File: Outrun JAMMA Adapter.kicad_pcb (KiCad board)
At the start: 2 copper layers, 111 x 86.6 mm, 31 parts, among them U1 LM386, U2 MCP4902, U3 ATMEGA328

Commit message: tooling holes
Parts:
- added REF**: ToolingHole_1.152mm, MountingHole:ToolingHole_1.152mm, F.Cu at (198.2, 79.4)
- added REF**: ToolingHole_1.152mm, MountingHole:ToolingHole_1.152mm, F.Cu at (99.8, 138.2)
- added REF**: ToolingHole_1.152mm, MountingHole:ToolingHole_1.152mm, F.Cu at (198.2, 138.2)

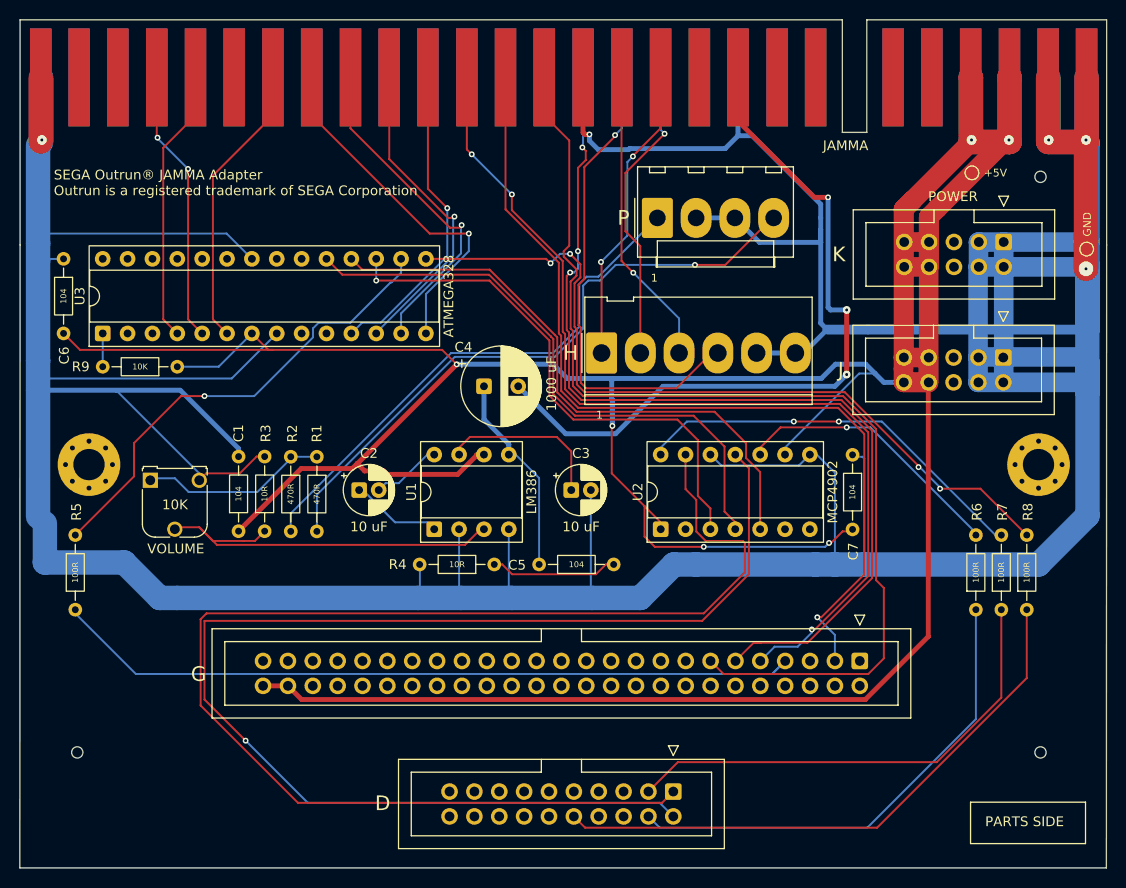
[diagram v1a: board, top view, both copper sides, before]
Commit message: remove tooling holes (0.2 precision), add space
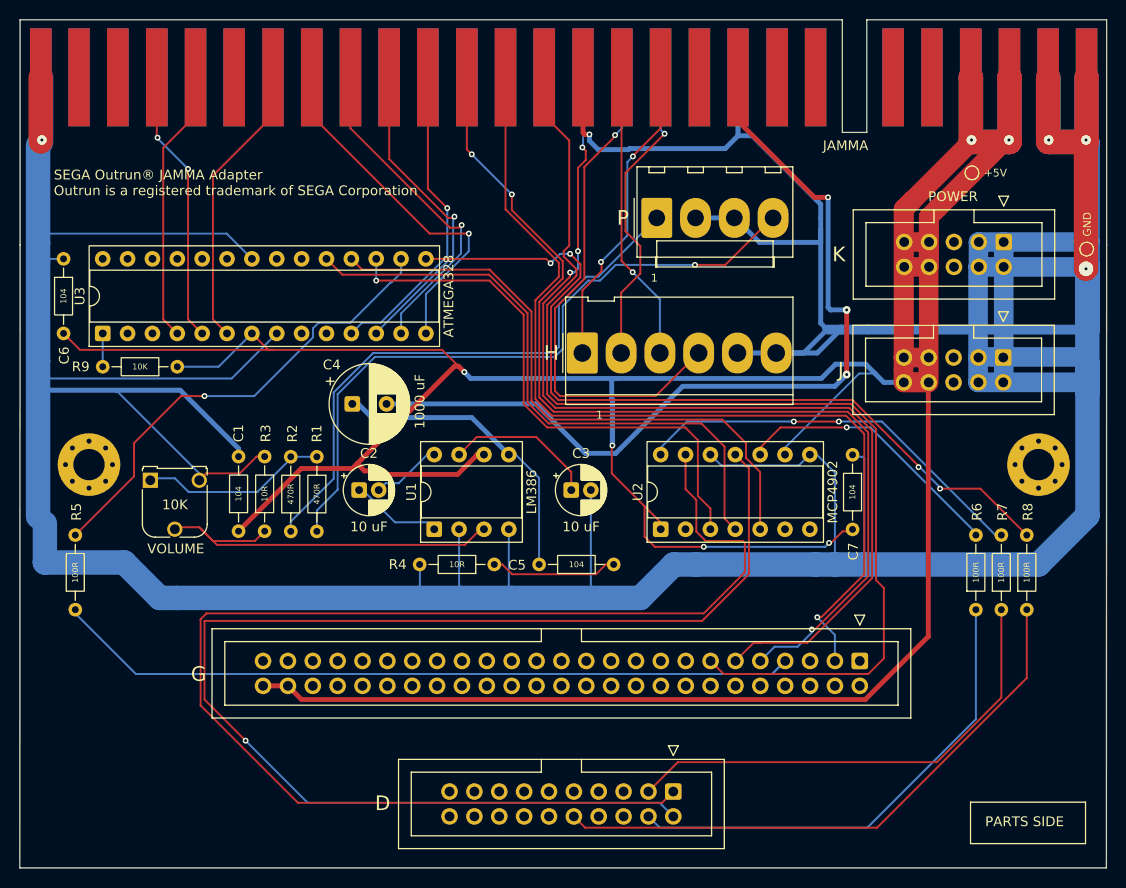
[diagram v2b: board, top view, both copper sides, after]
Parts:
- removed the REF** at (198.2, 79.4)
- removed the REF** at (99.8, 138.2)
- removed the REF** at (198.2, 138.2)
- moved C4 13.6 mm to (127.9, 102.6)
- moved H 1.96 mm to (151.4, 97.4)
- moved P 0.06 mm to (159.0, 83.6)
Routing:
- net SPKR+: track 74.8 -> 89.2 mm
- net PREAMP_OUT: track 20.9 -> 31.0 mm
- net GND: track 603.3 -> 612.9 mm
- net AUDIO_R: track 64.7 -> 69.4 mm
- net AUDIO_L: track 54.3 -> 59.0 mm
- net SERVICE: track 98.9 -> 102.9 mm
- net PB1: track 81.9 -> 85.9 mm
- net TEST: track 109.2 -> 113.2 mm
- net 1P_START: track 98.3 -> 102.3 mm
- net COIN_1: track 93.3 -> 97.3 mm
- net +5V: track 430.2 -> 433.2 mm
- net VID_CSYNC: track 48.9 -> 51.6 mm
- net U3_SCK_U2_SCK: track 60.8 -> 62.8 mm
- net U3_MOSI_U2_CS: track 54.8 -> 56.8 mm
- net U3_MISO_U2_SDI: track 60.8 -> 62.8 mm
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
